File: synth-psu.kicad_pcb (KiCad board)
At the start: 2 copper layers, 95 x 35 mm, 72 parts, among them J1 Conn_01x03_Male, J10 Conn_01x02_Male, J11 Conn_01x02_Male, J12 Conn_01x02_Male, J13 Conn_01x02_Male, J14 Conn_01x02_Male, J2 USB_C_Receptacle_16pin, J3 Conn_01x02_Male, J4 Conn_01x02_Male, J5 Conn_01x02_Male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

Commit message: mosfet footprint and lib, routed stusb4500
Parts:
- added JP1: SolderJumper_2_Open, Jumper:SolderJumper-2_P1.3mm_Open_TrianglePad1.0x1.5mm, F.Cu at (154.0, 83.5)
- added TP7: TestPoint, TestPoint:TestPoint_Pad_D1.5mm, F.Cu at (123.5, 85.5)
- added TP8: TestPoint, TestPoint:TestPoint_Pad_D1.5mm, F.Cu at (137.0, 66.0)
- Q1: footprint Package_TO_SOT_SMD:SOT-223-3_TabPin2 -> Package_SON:VSON-8_3.3x3.3mm_P0.65mm_NexFET
- moved Q1 21.7 mm to (140.6, 69.5)
- moved J1 20.3 mm to (130.0, 93.0), turned to 270 degrees
- moved C1 13.3 mm to (127.0, 77.4), turned to 180 degrees
- moved TP2 10.5 mm to (134.5, 74.5)
- moved TP6 10.1 mm to (135.5, 89.0)
- moved TP4 9.49 mm to (138.0, 89.0)
- moved R3 8.45 mm to (137.5, 79.6)
- moved TP3 8.25 mm to (133.0, 89.0)
- moved TP5 8.14 mm to (130.5, 89.0)
- moved C4 8.06 mm to (142.0, 66.0)
- moved R2 7.94 mm to (137.5, 77.2)
- moved C3 7.13 mm to (127.0, 75.0), turned to 180 degrees
- moved R6 6.73 mm to (140.0, 73.5)
- moved TP1 5.85 mm to (133.5, 78.0)
- moved U1 5.59 mm to (129.0, 81.5)
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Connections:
- net /reset renamed Net-(R1-Pad1)
- Q1 pad 1: +15V -> VBUS
- Q1 pad 3: Net-(Q1-Pad3) -> VBUS
- R3 pad 2: Net-(Q1-Pad3) -> Net-(Q1-Pad4)
- R4 pad 1: Net-(Q1-Pad3) -> Net-(Q1-Pad4)
- R5 pad 2: Net-(Q1-Pad3) -> Net-(Q1-Pad4)
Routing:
- net +15V: track 0.00 -> 58.2 mm
- net VBUS: track 0.00 -> 52.2 mm, vias 0 -> 2
- net /disch: track 0.00 -> 37.1 mm
- net /cc1: track 0.00 -> 16.4 mm
- net /cc2: track 0.00 -> 15.8 mm
- net Earth: track 0.00 -> 14.7 mm, vias 0 -> 9
- net Net-(Q1-Pad4): track 0.00 -> 13.5 mm
- net Net-(TP4-Pad1): track 0.00 -> 13.1 mm, vias 0 -> 2
- net Net-(C4-Pad2): track 0.00 -> 12.2 mm, vias 0 -> 2
- net /sda: track 0.00 -> 10.3 mm
- net /vbus_vs_disch: track 0.00 -> 10.2 mm
- net Net-(TP6-Pad1): track 0.00 -> 10.2 mm
- net /scl: track 0.00 -> 9.64 mm
- net Net-(TP3-Pad1): track 0.00 -> 8.52 mm
- net Net-(TP2-Pad1): track 0.00 -> 7.15 mm
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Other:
- net class power added: clearance 0.2, trace_width 0.5, via_dia 1, via_drill 0.6

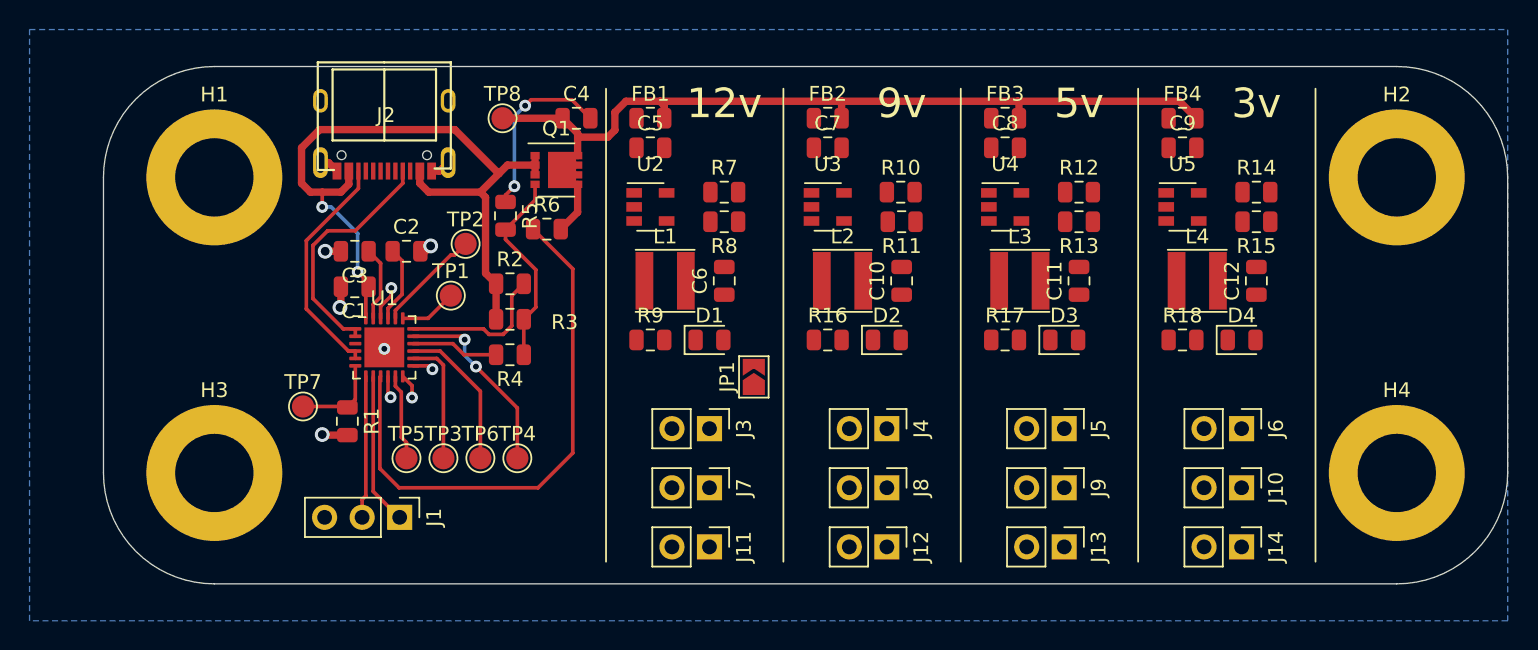
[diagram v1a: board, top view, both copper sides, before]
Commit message: change dc/dc to new part and did layout
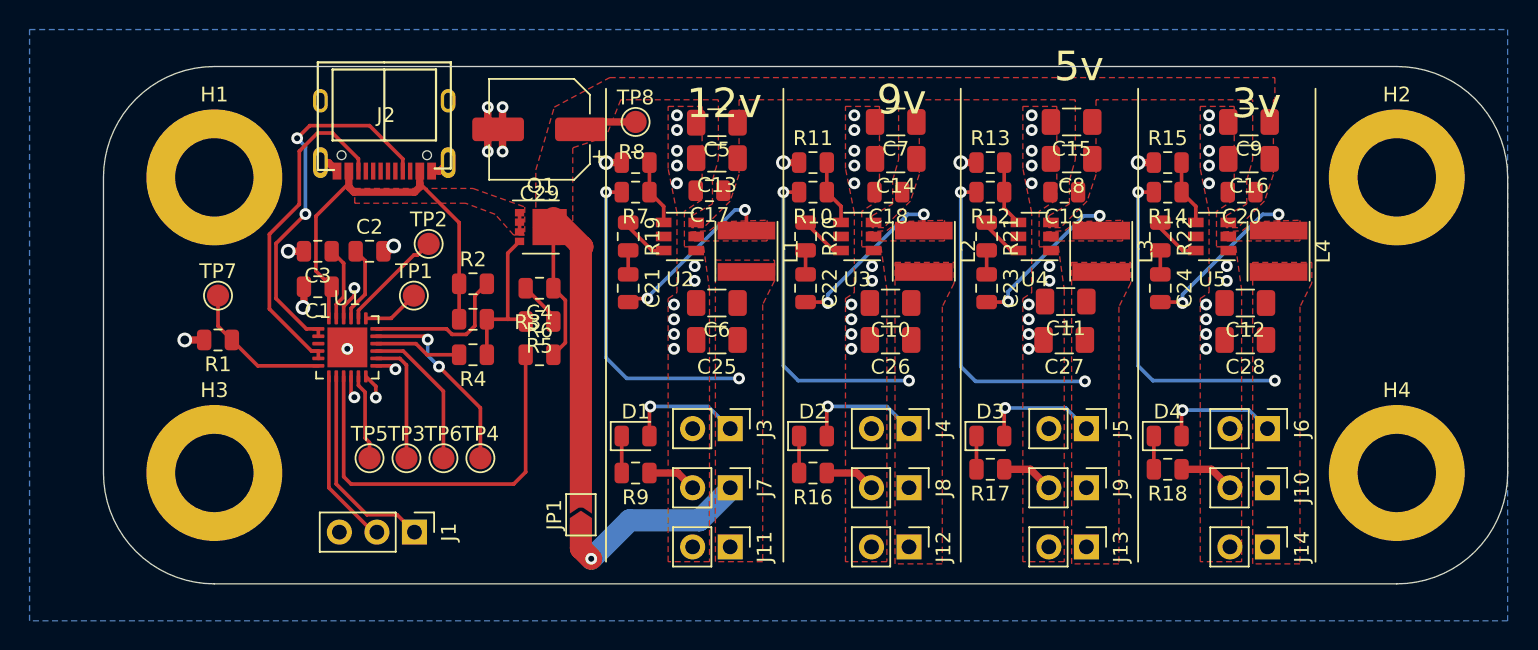
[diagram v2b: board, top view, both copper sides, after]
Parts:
- removed FB1, FB2, FB3, FB4: Ferrite_Bead_Small, Inductor_SMD:L_0805_2012Metric
- added C13: 10u, Capacitor_SMD:C_1206_3216Metric, F.Cu at (151.5, 68.7)
- added C14: 10u, Capacitor_SMD:C_1206_3216Metric, F.Cu at (163.6, 68.8)
- added C15: 10u, Capacitor_SMD:C_1206_3216Metric, F.Cu at (175.5, 66.2)
- added C16: 10u, Capacitor_SMD:C_1206_3216Metric, F.Cu at (187.5, 68.8)
- added C17: 100n, Capacitor_SMD:C_0805_2012Metric, F.Cu at (151.0, 70.9)
- added C18: 100n, Capacitor_SMD:C_0805_2012Metric, F.Cu at (163.1, 71.0)
- added C19: 100n, Capacitor_SMD:C_0805_2012Metric, F.Cu at (175.0, 71.0)
- added C20: 100n, Capacitor_SMD:C_0805_2012Metric, F.Cu at (187.0, 71.0)
- added C21: 100n, Capacitor_SMD:C_0805_2012Metric, F.Cu at (145.5, 77.5)
- added C22: 100n, Capacitor_SMD:C_0805_2012Metric, F.Cu at (157.5, 77.5)
- added C23: 100n, Capacitor_SMD:C_0805_2012Metric, F.Cu at (169.8, 77.5)
- added C24: 100n, Capacitor_SMD:C_0805_2012Metric, F.Cu at (181.5, 77.5)
- added C25: 22u, Capacitor_SMD:C_1206_3216Metric, F.Cu at (151.5, 81.0)
- added C26: 22u, Capacitor_SMD:C_1206_3216Metric, F.Cu at (163.2, 81.0)
- added C27: 22u, Capacitor_SMD:C_1206_3216Metric, F.Cu at (175.0, 81.0)
- added C28: 22u, Capacitor_SMD:C_1206_3216Metric, F.Cu at (187.2, 81.0)
- added C29: 100uf 16v, Capacitor_SMD:CP_Elec_6.3x5.9, F.Cu at (139.5, 66.8)
- added R19: 30R, Resistor_SMD:R_0805_2012Metric, F.Cu at (145.5, 74.0)
- added R20: 30R, Resistor_SMD:R_0805_2012Metric, F.Cu at (157.5, 74.0)
- added R21: 30R, Resistor_SMD:R_0805_2012Metric, F.Cu at (169.8, 74.0)
- added R22: 30R, Resistor_SMD:R_0805_2012Metric, F.Cu at (181.5, 74.0)
- C10, C11, C12, C6: footprint Capacitor_SMD:C_0805_2012Metric -> Capacitor_SMD:C_1206_3216Metric
- C5, C7, C8, C9: value 4.7u -> 10u; footprint Capacitor_SMD:C_0805_2012Metric -> Capacitor_SMD:C_1206_3216Metric
- L1: value 2.2uH -> 20uH
- L2: value 2.2uH -> 24uH
- L3: value 2.2uH -> 5.6uH
- L4: value 2.2uH -> 13uH
- R10: value 100k -> 102k
- R11, R13, R15, R8: value 120k -> 10k
- R12: value 100k -> 52.3k
- R14: value 100k -> 27.4k
- R7: value 100k -> 140k
- U2, U3, U4, U5: value TLV62568DBV -> TPS562200; footprint Package_TO_SOT_SMD:SOT-23-5 -> Package_TO_SOT_SMD:SOT-23-6
- moved JP1 15.0 mm to (142.3, 92.8)
- moved C4 11.8 mm to (139.5, 77.5), turned to 180 degrees
- moved R1 10.3 mm to (117.8, 81.0), turned to 180 degrees
- moved TP7 9.45 mm to (117.8, 78.0)
- moved R16 9.06 mm to (158.0, 90.0), turned to 180 degrees
- moved R9 9.06 mm to (146.0, 90.0), turned to 180 degrees
- moved TP8 9.00 mm to (146.0, 66.2)
- moved R17 8.81 mm to (170.0, 89.8), turned to 180 degrees
- moved R18 8.81 mm to (182.0, 89.8), turned to 180 degrees
- moved R6 8.51 mm to (139.5, 82.0)
- moved D1 8.20 mm to (146.0, 87.5)
- moved D2 8.20 mm to (158.0, 87.5)
- moved D3 8.20 mm to (170.0, 87.5)
- moved D4 8.20 mm to (182.0, 87.5)
- moved R5 7.51 mm to (139.5, 79.8), turned to 180 degrees
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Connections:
- C5 pad 1: Net-(C5-Pad1) -> +15V
- C7 pad 1: Net-(C7-Pad1) -> +15V
- C8 pad 1: Net-(C8-Pad1) -> +15V
- C9 pad 1: Net-(C9-Pad1) -> +15V
- L1 pad 1: Net-(L1-Pad1) -> /sw_12v
- L2 pad 1: Net-(L2-Pad1) -> /sw_9
- L3 pad 1: Net-(L3-Pad1) -> /sw_5
- L4 pad 1: Net-(L4-Pad1) -> /sw_3
- U2 pad 1: Net-(C5-Pad1) -> Earth
- U2 pad 2: Earth -> /sw_12v
- U2 pad 3: Net-(L1-Pad1) -> +15V
- U2 pad 4: Net-(C5-Pad1) -> Net-(R7-Pad1)
- U2 pad 5: Net-(R7-Pad1) -> Net-(U2-Pad5)
- U3 pad 1: Net-(C7-Pad1) -> Earth
- U3 pad 2: Earth -> /sw_9
- U3 pad 3: Net-(L2-Pad1) -> +15V
- U3 pad 4: Net-(C7-Pad1) -> Net-(R10-Pad1)
- U3 pad 5: Net-(R10-Pad1) -> Net-(U3-Pad5)
- U4 pad 1: Net-(C8-Pad1) -> Earth
- U4 pad 2: Earth -> /sw_5
- U4 pad 3: Net-(L3-Pad1) -> +15V
- U4 pad 4: Net-(C8-Pad1) -> Net-(R12-Pad1)
- U4 pad 5: Net-(R12-Pad1) -> Net-(U4-Pad5)
- U5 pad 1: Net-(C9-Pad1) -> Earth
- U5 pad 2: Earth -> /sw_3
- U5 pad 3: Net-(L4-Pad1) -> +15V
- U5 pad 4: Net-(C9-Pad1) -> Net-(R14-Pad1)
- U5 pad 5: Net-(R14-Pad1) -> Net-(U5-Pad5)
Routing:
- net +12V: track 0.00 -> 43.9 mm, vias 0 -> 4
- net +3V0: track 0.00 -> 30.5 mm, vias 0 -> 3
- net +9V: track 0.00 -> 29.9 mm, vias 0 -> 3
- net +5V: track 0.00 -> 29.7 mm, vias 0 -> 3
- net +15V: track 58.2 -> 32.8 mm
- net Earth: track 14.7 -> 39.5 mm, vias 9 -> 61
- net VBUS: track 52.2 -> 30.2 mm, vias 2 -> 0
- net /sw_12v: track 0.00 -> 12.0 mm, vias 0 -> 2
- net /sw_9: track 0.00 -> 11.9 mm, vias 0 -> 2
- net /sw_3: track 0.00 -> 11.9 mm, vias 0 -> 2
- net /sw_5: track 0.00 -> 11.5 mm, vias 0 -> 2
- net /disch: track 37.1 -> 27.6 mm
- net Net-(C4-Pad2): track 12.2 -> 3.03 mm, vias 2 -> 0
- net /cc1: track 16.4 -> 25.4 mm, vias 0 -> 2
- net /cc2: track 15.8 -> 22.6 mm
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- added copper zone on F.Cu, net +12V
- added copper zone on F.Cu, net +15V
- added copper zone on F.Cu, net +3V0
- added copper zone on F.Cu, net +5V
- added copper zone on F.Cu, net +9V
- added copper zone on F.Cu, net /sw_12v
- added copper zone on F.Cu, net /sw_3
- added copper zone on F.Cu, net /sw_5
- added copper zone on F.Cu, net /sw_9
- added copper zone on F.Cu, net Earth
- added copper zone on F.Cu, net VBUS

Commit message: removed 1 set of supply sockets to fit molex polarised kk, silk screen
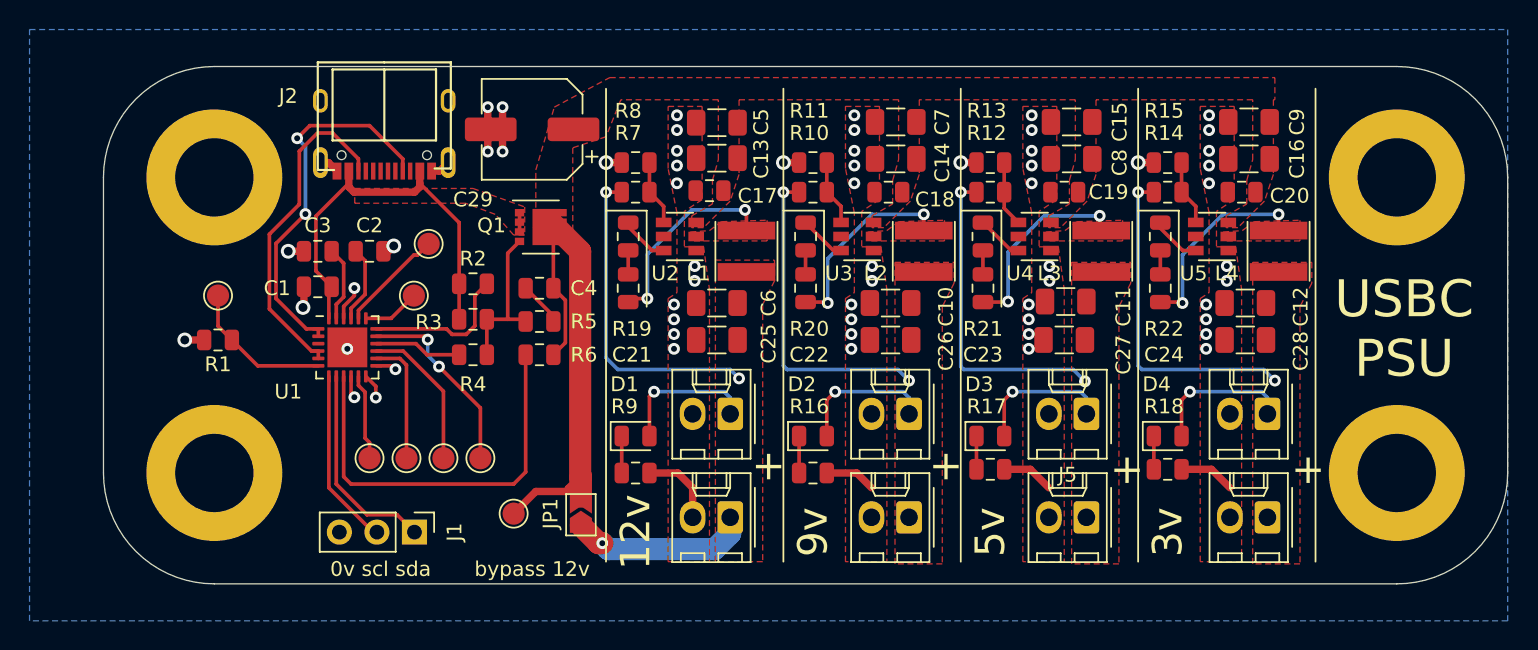
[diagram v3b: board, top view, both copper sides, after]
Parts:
- removed J11, J12, J13, J14: Conn_01x02_Male, Connector_PinHeader_2.54mm:PinHeader_1x02_P2.54mm_Vertical
- J10, J3, J4, J5, J6, J7, J8, J9: footprint Connector_PinHeader_2.54mm:PinHeader_1x02_P2.54mm_Vertical -> Connector_Molex:Molex_KK-254_AE-6410-02A_1x02_P2.54mm_Vertical
- moved TP8 27.8 mm to (137.8, 92.8)
- moved J10 2.00 mm to (188.8, 93.0), turned to 180 degrees
- moved J7 2.00 mm to (152.4, 93.0), turned to 180 degrees
- moved J8 2.00 mm to (164.5, 93.0), turned to 180 degrees
- moved J9 2.00 mm to (176.5, 93.0), turned to 180 degrees
- moved J3 1.00 mm to (152.4, 86.0), turned to 180 degrees
- moved J4 1.00 mm to (164.5, 86.0), turned to 180 degrees
- moved J5 1.00 mm to (176.5, 86.0), turned to 180 degrees
- moved J6 1.00 mm to (188.8, 86.0), turned to 180 degrees
- moved C29 0.50 mm to (139.0, 66.8)
- moved C23 0.25 mm to (169.5, 77.5)
- moved R21 0.25 mm to (169.5, 74.0)
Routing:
- net +15V: track 32.8 -> 36.2 mm
- net Earth: track 39.5 -> 41.5 mm
- net /sw_12v: track 12.0 -> 13.7 mm
- net +3V0: track 30.5 -> 32.2 mm
- net /sw_5: track 11.5 -> 13.1 mm
- net /sw_3: track 11.9 -> 13.5 mm
- net +5V: track 29.7 -> 31.2 mm
- net /sw_9: track 11.9 -> 13.4 mm
- net +9V: track 29.9 -> 31.2 mm
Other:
- board text added: "$git$"
- board text added: "+"
- board text added: "0v scl sda"
- board text added: "2 approved DRC errors"
- board text added: "USBC PSU"
- board text added: "bypass 12v"
- board text added: "github.com/mattvenn/usbc-synth-psu"
